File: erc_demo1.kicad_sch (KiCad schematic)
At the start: 4 parts, among them J1 Conn_01x01, J2 Conn_01x01, J3 Conn_01x02, J6 Conn_01x02

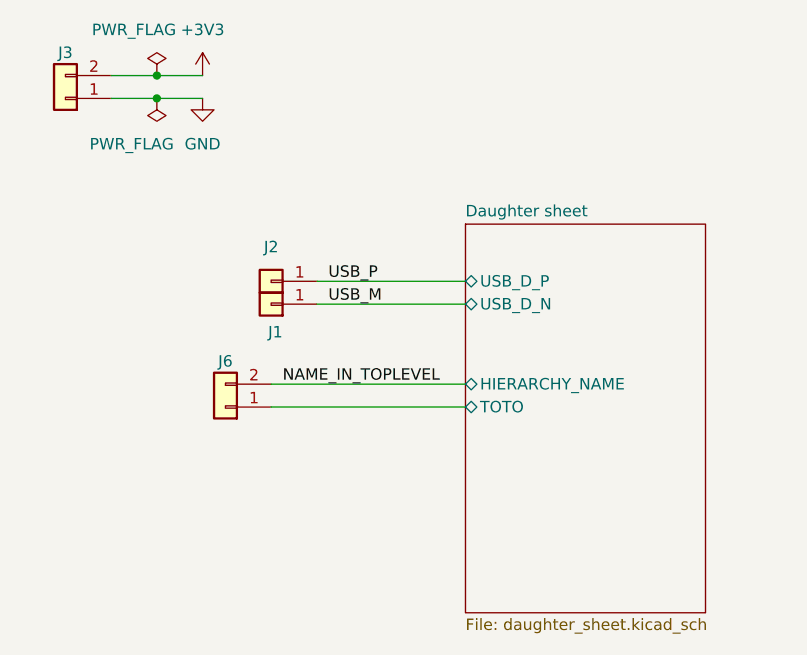
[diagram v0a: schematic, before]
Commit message: feat: add a hierarchy name demo
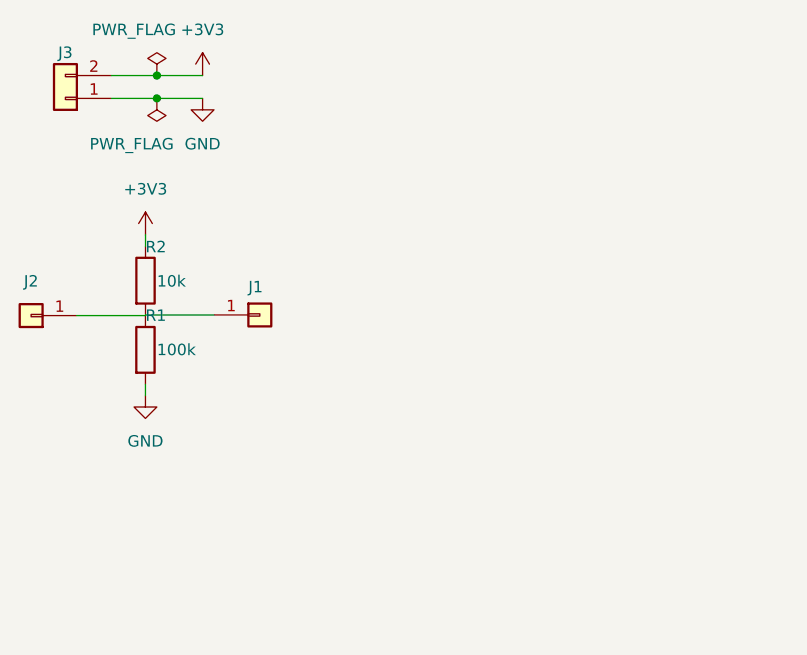
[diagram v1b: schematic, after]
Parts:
- removed J6: Conn_01x02, Connector_PinHeader_2.54mm:PinHeader_1x02_P2.54mm_Vertical, symbol Connector_Generic:Conn_01x02
- added R1: 100k, Resistor_SMD:R_0603_1608Metric, symbol Device:R
- added R2: 10k, Resistor_SMD:R_0603_1608Metric, symbol Device:R
- J3: footprint Connector_PinHeader_2.54mm:PinHeader_1x02_P2.54mm_Vertical -> (none)
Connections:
- net +3V3: now also R2.1
- net GND: now also R1.2
- net USB_M: no longer names the net of J1.1 (Pin_1)
- net USB_M: now also R2.2
- net USB_P: no longer names the net of J2.1 (Pin_1)
- net USB_P: now also R1.1
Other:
- removed sheet Daughter sheet
- moved on the sheet: J1, J2
